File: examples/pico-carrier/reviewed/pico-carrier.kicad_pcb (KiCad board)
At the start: 2 copper layers, 88 x 62 mm, 9 parts, among them J1 5V IN, J3 GP0-GP15, J4 GP16-GP28, PWR, U1 Pico

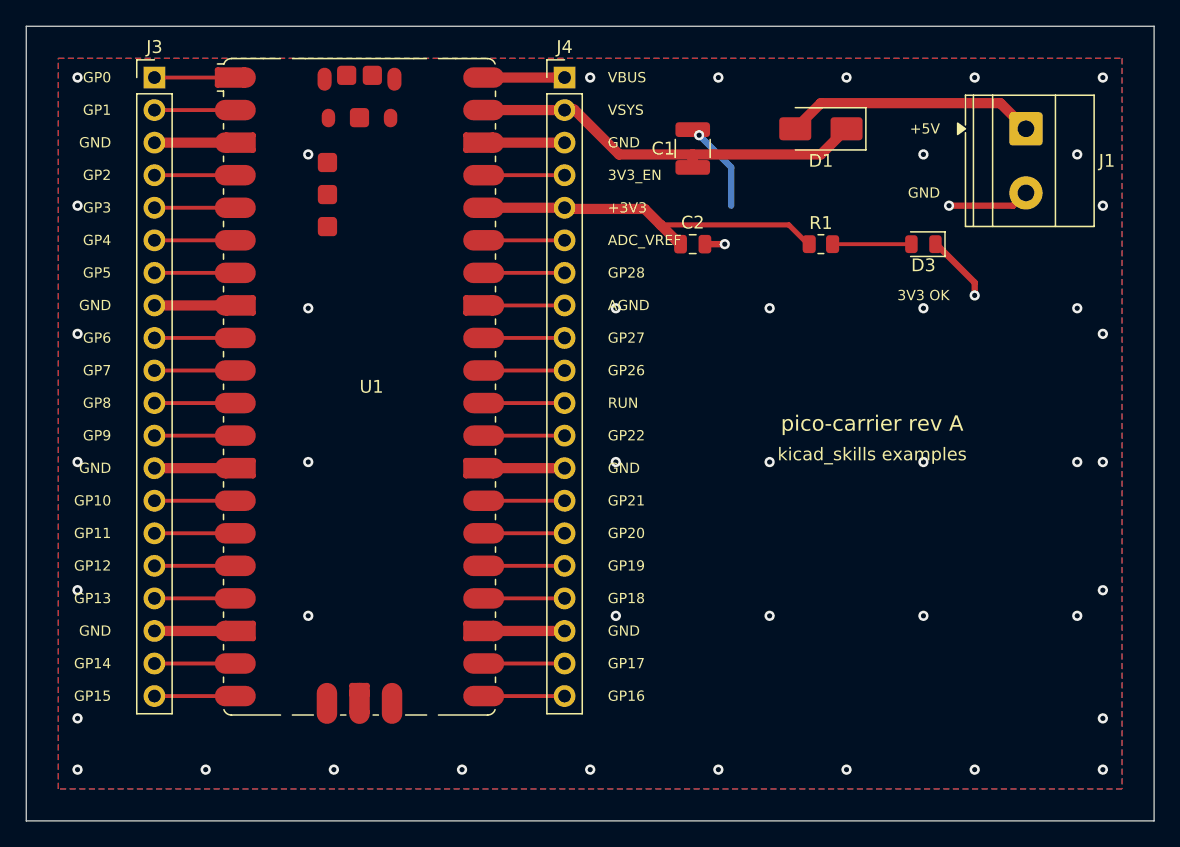
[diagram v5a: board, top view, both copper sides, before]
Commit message: Treat the ground plane as part of the drawing
Six reviewer circles, five of them the plane seen from different corners.
The pour now stops 1.2 mm inside the outline so an edge-hugging trace
keeps shell copper outside it; dead-end tongues narrower than 0.9 mm
retract instead of tapering to an acid-trap point in a bent corner; every
piece of the front pour over 8 mm2 holds a stitching via of its own,
placed before the orphan drop so a fenced-off strip gets a via instead of
staying a blank; and zone clearance comes down from 0.4 to 0.25, which is
what lets the plane flow between a 2.54 mm header's pins instead of
slotting the board top to bottom.

The round-twelve tee learns one manner: within two millimetres of the
goal it stands aside, so a rail flows through a bypass capacitor's pad
instead of feeding it by a stub - the carrier's bulk capacitor also moves
onto the VSYS run it was a millimetre south of. And
readability.margin_intrusion now measures symbol fields, power symbols
included: zero findings across KiCad's 18 demo sheets, one real catch on
our own motor sheet, whose power connector - like the FPGA board's -
moves in from the sheet edge so its printed name clears the frame.

Co-Authored-By: Claude Fable 5 <noreply@anthropic.com>
Claude-Session: https://claude.ai/code/session_01DUj7Ltu92tWg159mCSacwY
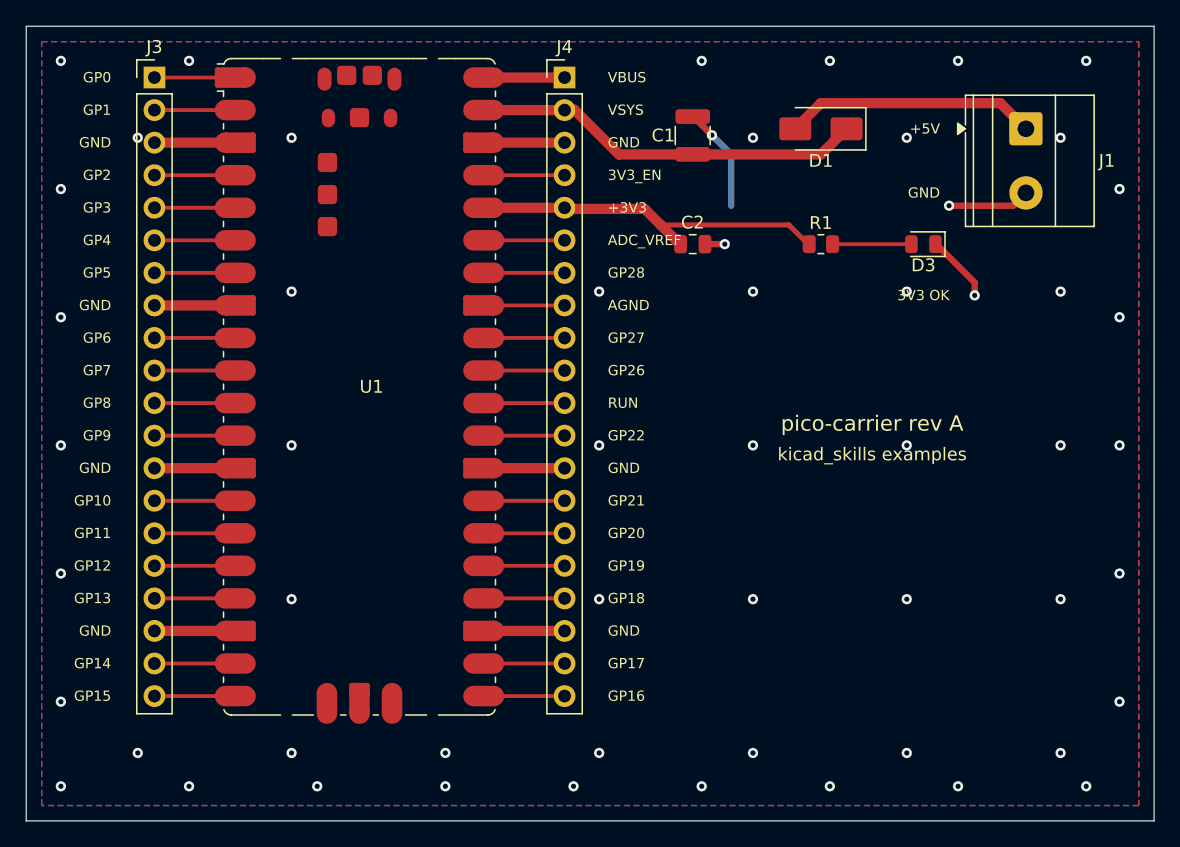
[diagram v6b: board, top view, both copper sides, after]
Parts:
- moved C1 1.02 mm to (152.0, 68.5)
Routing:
- net /VSYS: track 31.6 -> 30.6 mm
- net GND: track 64.7 -> 65.7 mm, vias 47 -> 56
